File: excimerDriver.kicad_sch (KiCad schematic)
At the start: 38 parts, among them IC3 INA210, IC6 STM32G071KBT6, J1 B08B-XASK-1-A_LF__SN_, J2 TC2050-IDC, J3 BM02B-SRSS-TB_LF__SN_, J4 BM02B-SRSS-TB_LF__SN_, J6 640445-2, Q3 BSS138

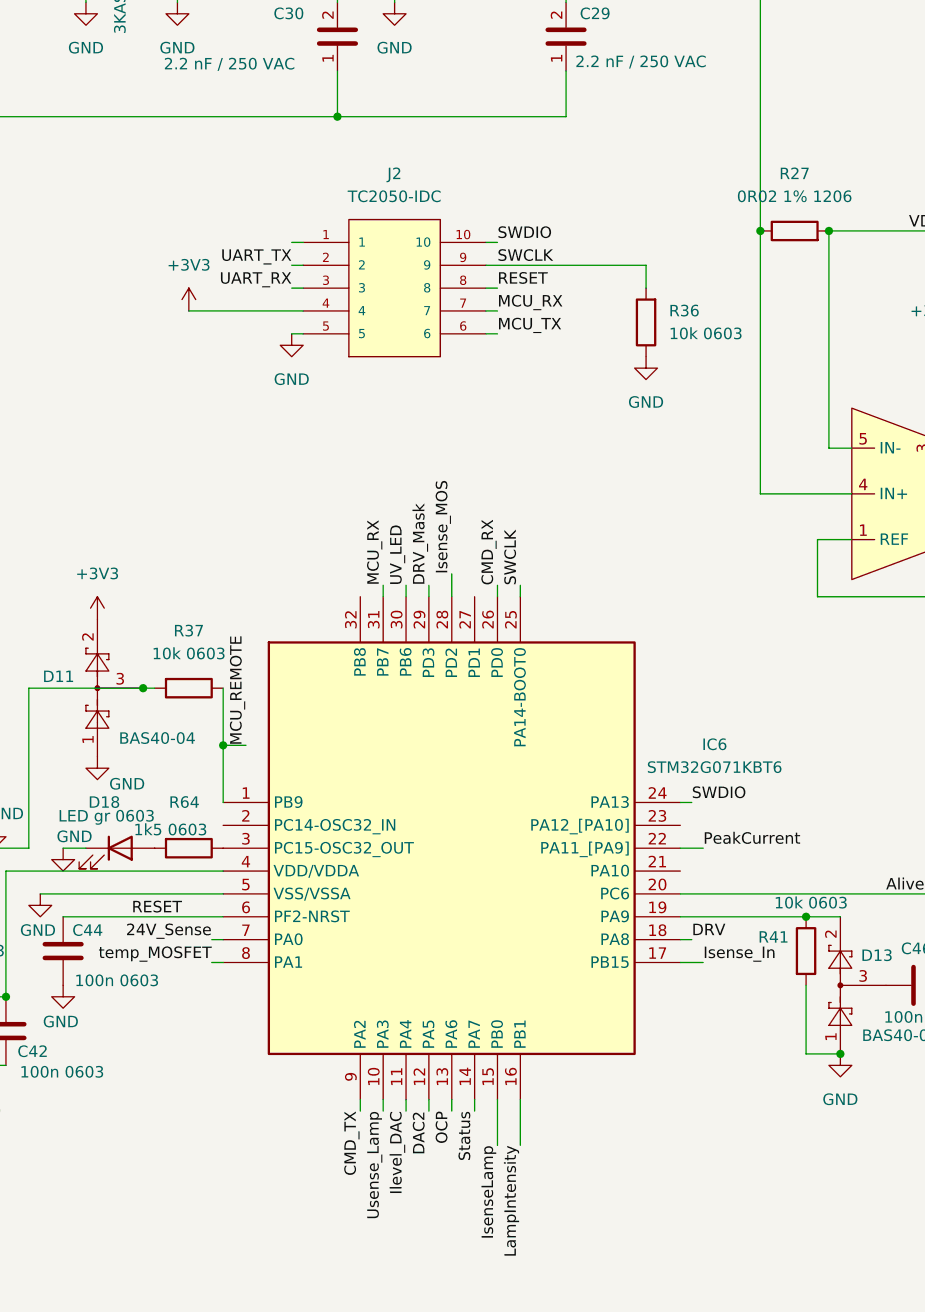
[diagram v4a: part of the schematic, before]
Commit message: routing single side done
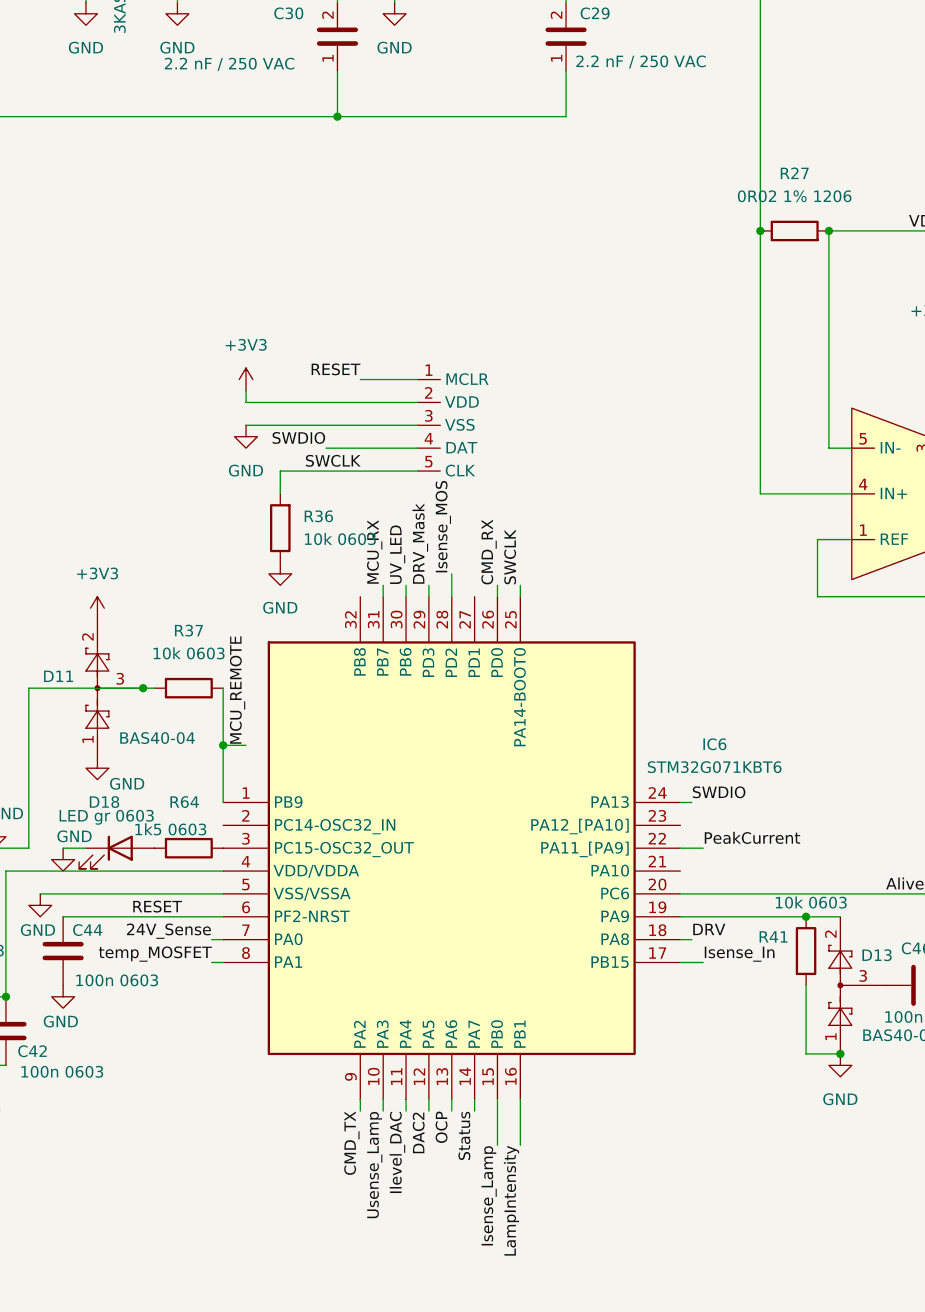
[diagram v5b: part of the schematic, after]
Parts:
- removed J2: TC2050-IDC, Hansmann:TAG-CONNECT_TC2050-IDC, symbol Hansmann:TC2050-IDC
- added U4: Prog, Hansmann:Prog_St, symbol Hansmann:Prog_ST
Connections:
- net IsenseLamp is gone; now on net Isense_Lamp: IC6.15 (PB0)
- net +3V3: now also U4.2 (VDD)
- net GND: now also U4.3 (VSS)
- net RESET: now also U4.1 (MCLR)
- net SWCLK: now also U4.5 (CLK)
- net SWDIO: now also U4.4 (DAT)
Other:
- moved on the sheet: R36

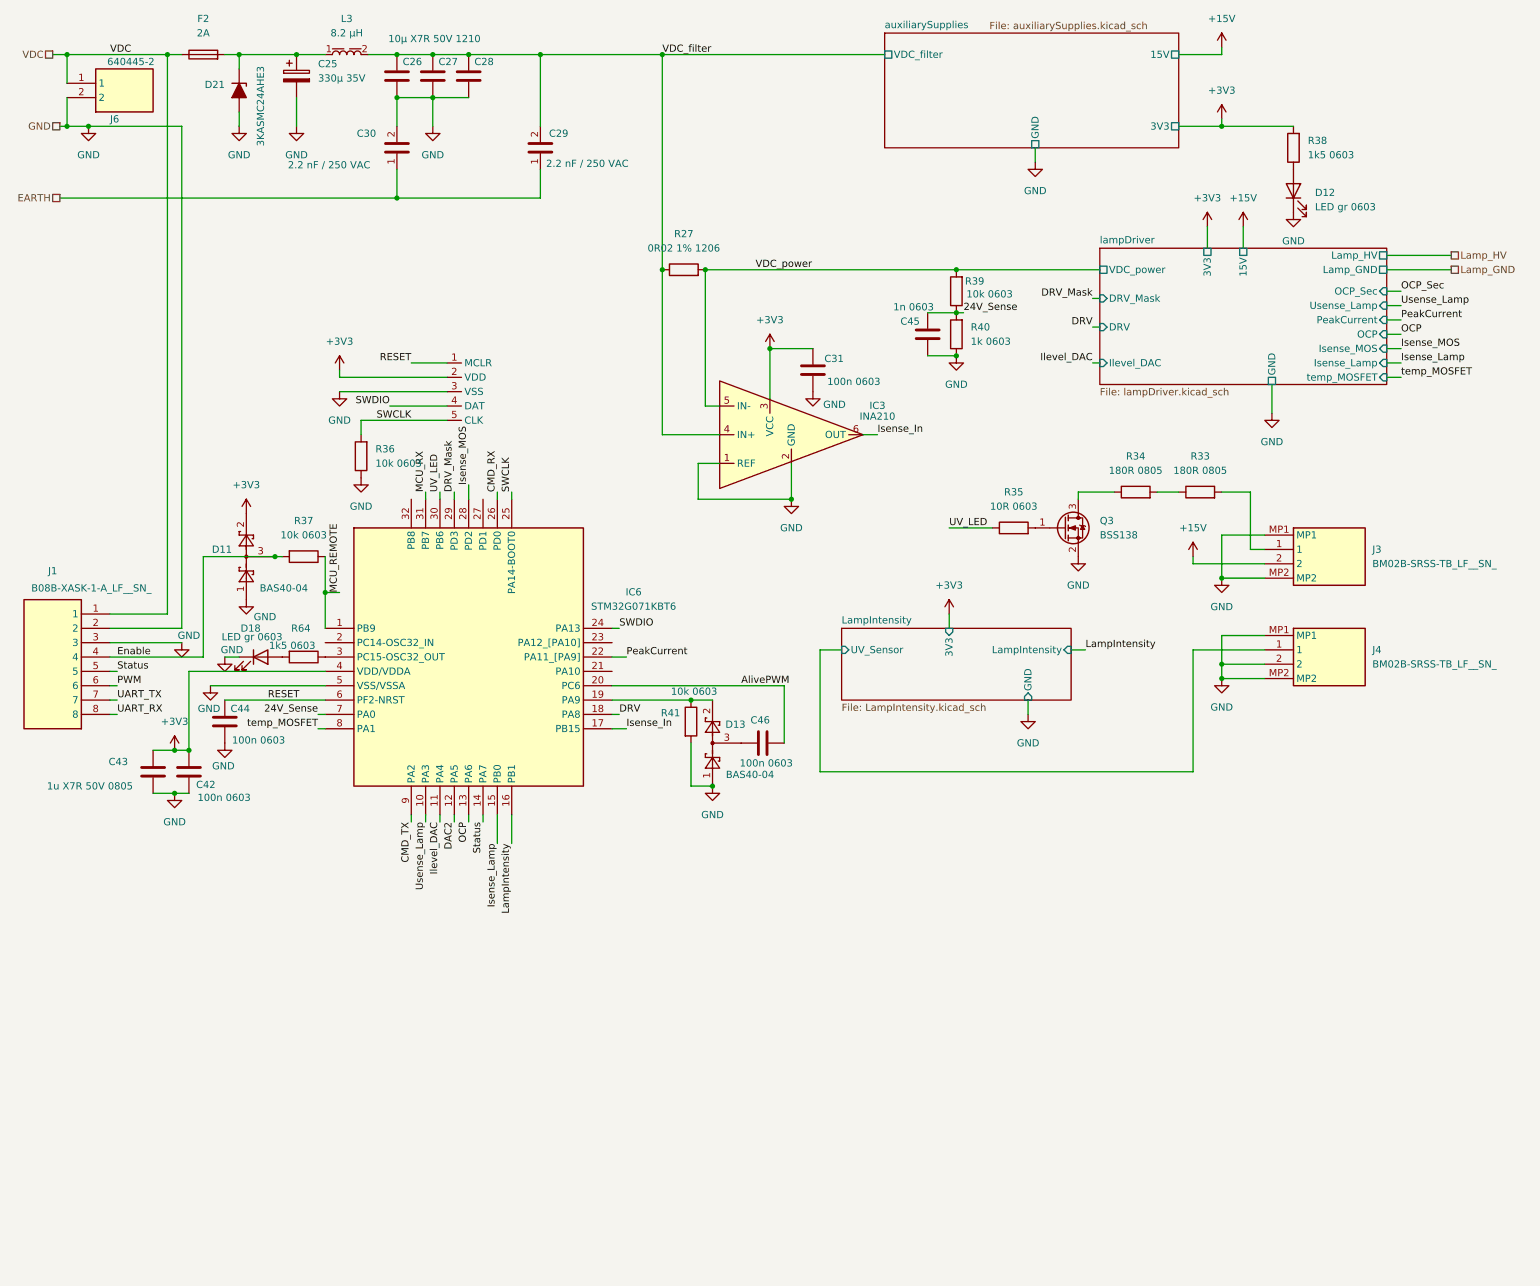
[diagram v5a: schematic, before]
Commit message: initial version of excimer driver PCB
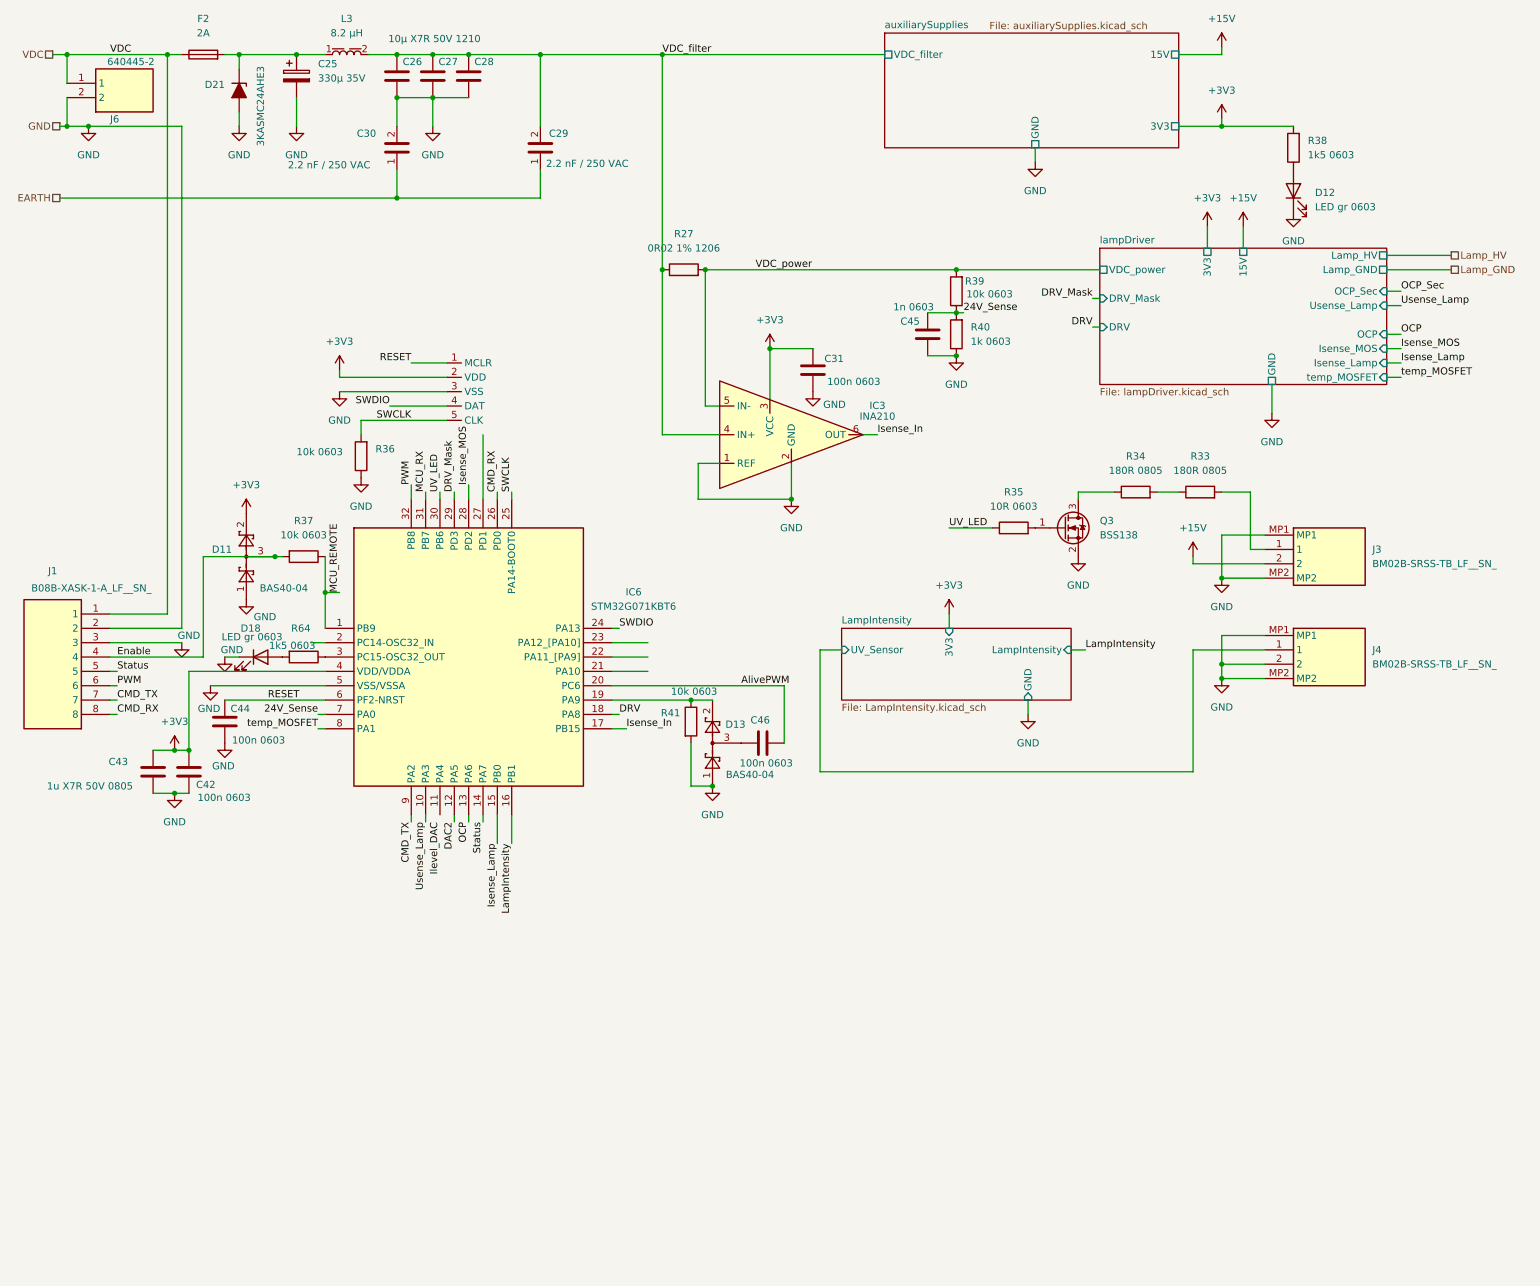
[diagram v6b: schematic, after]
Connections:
- net UART_RX is gone; now on net CMD_RX: J1.8
- net UART_TX is gone; now on net CMD_TX: J1.7
- net Ilevel_DAC: no longer IC6.11 (PA4)
- net PWM: now also IC6.32 (PB8)
- net PeakCurrent: no longer names the net of IC6.22 (PA11_[PA9])
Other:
- sheet lampDriver ports: added none; removed Ilevel_DAC, PeakCurrent

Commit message: error correction
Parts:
- added U3: LM2902, Package_SO:TSSOP-14_4.4x5mm_P0.65mm, symbol Amplifier_Operational:LM2902
- renumbered C25 to C110
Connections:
- net GND: now also U3.5 (+)
